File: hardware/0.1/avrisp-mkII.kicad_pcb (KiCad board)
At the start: 2 copper layers, 5 parts

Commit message: layout done
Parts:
- removed LOGO5: 4-Layer-Check, josh-logos:4-layer-check
- added C1: 1u, Capacitor_SMD:C_0603_1608Metric, F.Cu at (141.1, 104.6)
- added C10: 100n, Capacitor_SMD:C_0603_1608Metric, F.Cu at (162.1, 113.9)
- added C11: 10u, Capacitor_SMD:C_0603_1608Metric, F.Cu at (165.1, 113.9)
- added C12: 100n, Capacitor_SMD:C_0603_1608Metric, F.Cu at (168.0, 100.9)
- added C2: 1u, Capacitor_SMD:C_0603_1608Metric, F.Cu at (147.2, 105.4)
- added C3: 100n, Capacitor_SMD:C_0603_1608Metric, F.Cu at (151.7, 104.6)
- added C4: 100u, Capacitor_Tantalum_SMD:CP_EIA-3216-10_Kemet-I, F.Cu at (149.8, 105.4)
- added C5: 22P, Capacitor_SMD:C_0603_1608Metric, F.Cu at (154.8, 113.6)
- added C6: 22P, Capacitor_SMD:C_0603_1608Metric, F.Cu at (160.6, 113.9)
- added C7: 1u, Capacitor_SMD:C_0603_1608Metric, F.Cu at (154.0, 105.3)
- added C8: 100n, Capacitor_SMD:C_0603_1608Metric, F.Cu at (154.0, 111.3)
- added C9: 100n, Capacitor_SMD:C_0603_1608Metric, F.Cu at (154.0, 109.8)
- added D1: 1N4148, Diode_SMD:D_SOD-323, F.Cu at (160.3, 100.4)
- added D2: PWR, LED_SMD:LED_0603_1608Metric, F.Cu at (148.1, 114.3)
- added D3: STAT, LED_SMD:LED_0603_1608Metric, F.Cu at (144.7, 114.3)
- added D4: BAT54C, Package_TO_SOT_SMD:SOT-23, F.Cu at (168.6, 108.0)
- added D5: ACT, LED_SMD:LED_0603_1608Metric, F.Cu at (146.4, 114.3)
- added D6: BAT54C, Package_TO_SOT_SMD:SOT-23, F.Cu at (168.6, 111.5)
- added F1: 100mA, josh-passives-smt:Fuse_0805_2012Metric, F.Cu at (165.5, 100.4)
- added FB1: 600R, josh-passives-smt:Ferrite_Bead_0603, F.Cu at (139.5, 104.6)
- added FB2: 600R, josh-passives-smt:Ferrite_Bead_0603, F.Cu at (147.2, 103.8)
- added J1: USB_C_Receptacle_USB2.0, josh-connectors:USB_C_U262-161N-4BVC11, F.Cu at (133.9, 107.6)
- added J2: 2.54 THT, Connector_PinHeader_2.54mm:PinHeader_1x03_P2.54mm_Vertical, F.Cu at (140.0, 101.2)
- added J3: 2.54 THT, Connector_PinHeader_2.54mm:PinHeader_1x03_P2.54mm_Vertical, F.Cu at (148.7, 101.2)
- added J4: AVR ISP, Connector_IDC:IDC-Header_2x03_P2.54mm_Vertical, F.Cu at (174.0, 105.0)
- added JP1: VCC_SEL, Jumper:SolderJumper-3_P1.3mm_Bridged12_Pad1.0x1.5mm, B.Cu at (143.7, 107.1)
- added R1: 5K1, Resistor_SMD:R_0603_1608Metric, F.Cu at (140.3, 106.9)
- added R2: 5K1, Resistor_SMD:R_0603_1608Metric, F.Cu at (143.2, 114.3)
- added R3: 10K, Resistor_SMD:R_0603_1608Metric, F.Cu at (154.0, 103.8)
- added R4: 100R, Resistor_SMD:R_0603_1608Metric, F.Cu at (157.1, 100.6)
- added R5: 22R, Resistor_SMD:R_0603_1608Metric, F.Cu at (154.0, 106.8)
- added R6: 22R, Resistor_SMD:R_0603_1608Metric, F.Cu at (154.0, 108.3)
- added R8: 1M, Resistor_SMD:R_0603_1608Metric, F.Cu at (163.6, 113.9)
- added R9: 200R, Resistor_SMD:R_0603_1608Metric, F.Cu at (169.5, 100.9)
- added RN1: 1K, Resistor_SMD:R_Array_Convex_4x0603, F.Cu at (152.1, 113.7)
- added RN2: 1K, Resistor_SMD:R_Array_Convex_4x0603, F.Cu at (168.7, 104.4)
- added SW1: RST, josh-buttons-switches:Panasonic_EVQPUL_EVQPUC, B.Cu at (141.8, 113.9)
- added SW2: SW_Push, josh-buttons-switches:Panasonic_EVQPUL_EVQPUC, B.Cu at (149.7, 113.9)
- added U1: USBLC6-2SC6, Package_TO_SOT_SMD:SOT-23-6, F.Cu at (140.7, 109.5)
- added U2: AP2112K-3.3, Package_TO_SOT_SMD:SOT-23-5, F.Cu at (143.8, 104.8)
- added U3: MCP130-xxxxTT, Package_TO_SOT_SMD:SOT-23, F.Cu at (147.0, 107.9)
- added U4: AT90USB162-16AU, Package_QFP:TQFP-32_7x7mm_P0.8mm, F.Cu at (160.9, 106.7)
- added Y1: 16MHz, josh-oscillators:Crystal_SMD_3225-4Pin_3.2x2.5mm, F.Cu at (157.7, 113.7)
- LOGO1: renamed from LOGO3; moved to B.Cu
- LOGO2: renamed from LOGO4; moved to B.Cu
- LOGO3: renamed from LOGO1; moved to B.Cu
- LOGO4: renamed from LOGO2; moved to B.Cu
- moved LOGO4 90.4 mm to (132.3, 107.0), turned to 270 degrees
- moved LOGO2 88.4 mm to (175.2, 111.6), turned to 180 degrees
- moved LOGO1 85.9 mm to (172.2, 98.8), turned to 180 degrees
- moved LOGO3 78.5 mm to (174.8, 112.6), turned to 180 degrees
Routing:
- net VCC: track 0.00 -> 51.0 mm, vias 0 -> 6
- net Net-(R4-Pad1): track 0.00 -> 46.8 mm, vias 0 -> 2
- net GND: track 0.00 -> 45.5 mm, vias 0 -> 17
- net Net-(C11-Pad1): track 0.00 -> 41.7 mm, vias 0 -> 3
- net /USB_PWR_DET: track 0.00 -> 41.6 mm, vias 0 -> 3
- net /V_TARGET: track 0.00 -> 35.4 mm
- net /ICSP_RST: track 0.00 -> 21.7 mm
- net /RST: track 0.00 -> 21.3 mm, vias 0 -> 2
- net /LED_USB_PWR: track 0.00 -> 19.4 mm, vias 0 -> 2
- net +5V: track 0.00 -> 18.8 mm, vias 0 -> 1
- net /LED_ACTIVITY: track 0.00 -> 17.9 mm, vias 0 -> 2
- net /LED_READY: track 0.00 -> 17.0 mm, vias 0 -> 2
- net /ICSP_MOSI: track 0.00 -> 16.3 mm, vias 0 -> 1
- net Net-(D3-Pad2): track 0.00 -> 14.7 mm, vias 0 -> 2
- net /USB_D+: track 0.00 -> 13.3 mm
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- added copper zone on B.Cu, net GND
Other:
- board outline added: 51.2 x 17 mm
- board text added: "3V3"
- board text added: "5V0"
- board text added: "GND"
- board text added: "HWB"
- board text added: "MISO"
- board text added: "MOSI"
- board text added: "OFF"
- board text added: "ON"
- board text added: "PWR"
- board text added: "RST"
- board text added: "SCK"
- board text added: "TGT"
- board text added: "VCC"
- board text added: "VREF"
- board text added: "nRST"

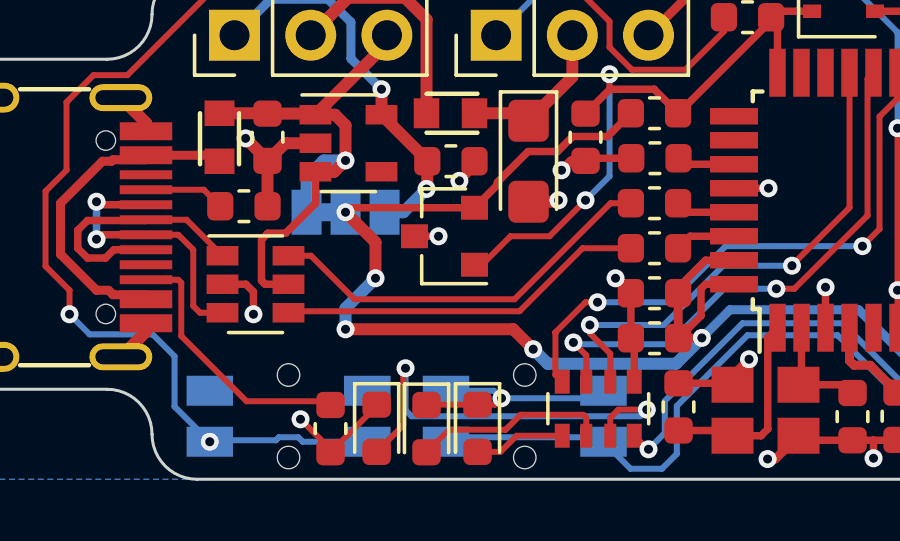
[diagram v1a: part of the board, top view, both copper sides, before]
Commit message: adding silk
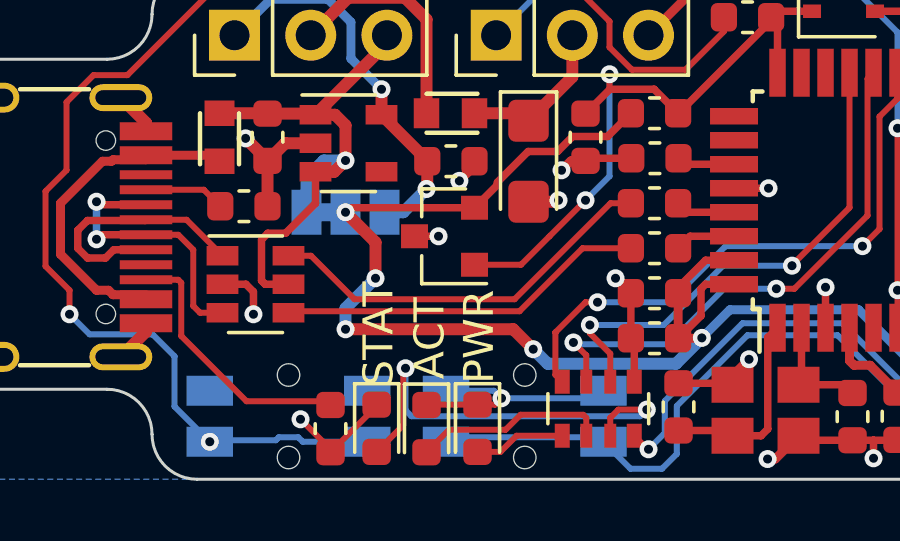
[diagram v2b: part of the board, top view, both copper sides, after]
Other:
- board text added: "ACT"
- board text added: "STAT"

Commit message: update readme
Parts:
- moved LOGO4 1.62 mm to (133.8, 107.6)
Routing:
- net VCC: track 51.0 -> 48.6 mm
- net Net-(D2-Pad2): track 3.05 -> 4.25 mm
- net Net-(D3-Pad2): track 14.7 -> 14.1 mm
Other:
- board text added: "READY"
- board text added: "TGT PWR"
- board text removed: "STAT"
